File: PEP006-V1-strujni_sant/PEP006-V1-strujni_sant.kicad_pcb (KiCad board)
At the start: 2 copper layers, 45 x 45 mm, 17 parts, among them J1 Screw_Terminal_01x02, J2 Conn_01x02_Pin, J3 Conn_01x02_Pin, J4 Conn_01x02_Pin

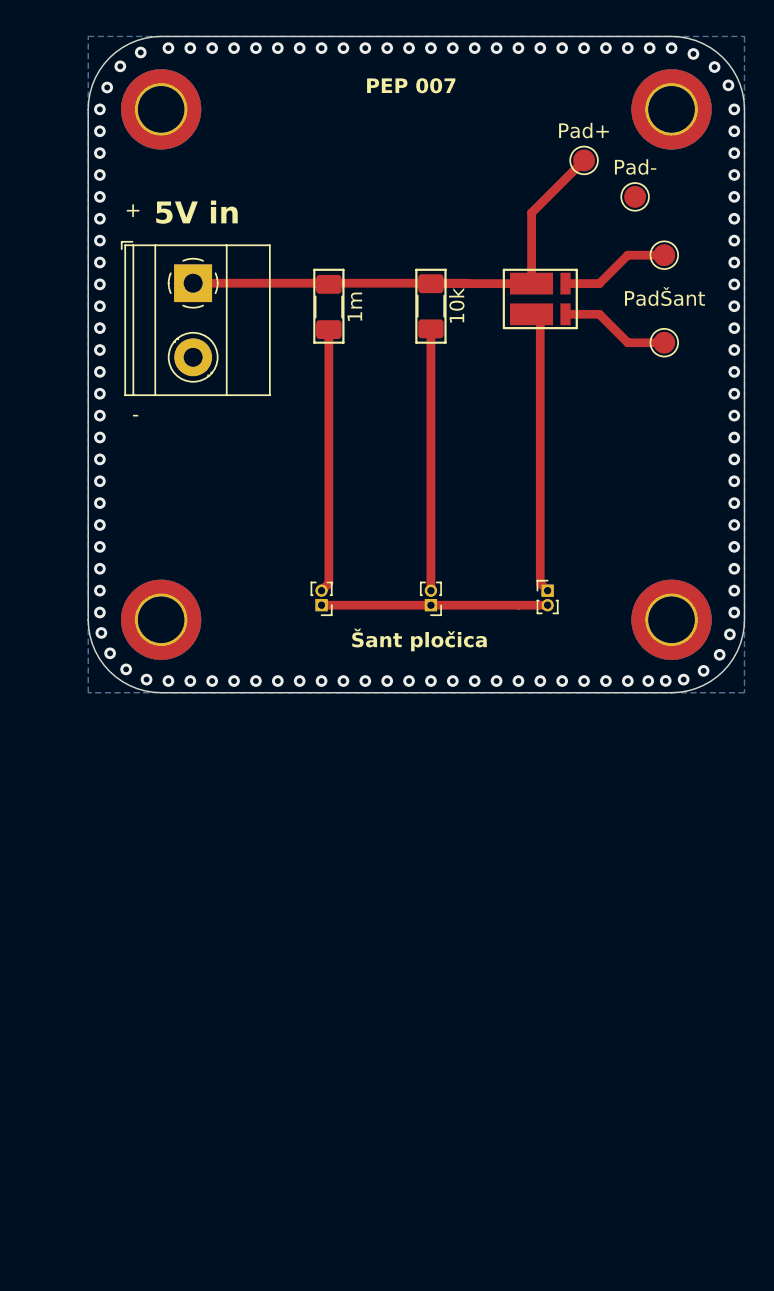
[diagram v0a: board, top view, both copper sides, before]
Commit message: PEP006 and PEP009 update.
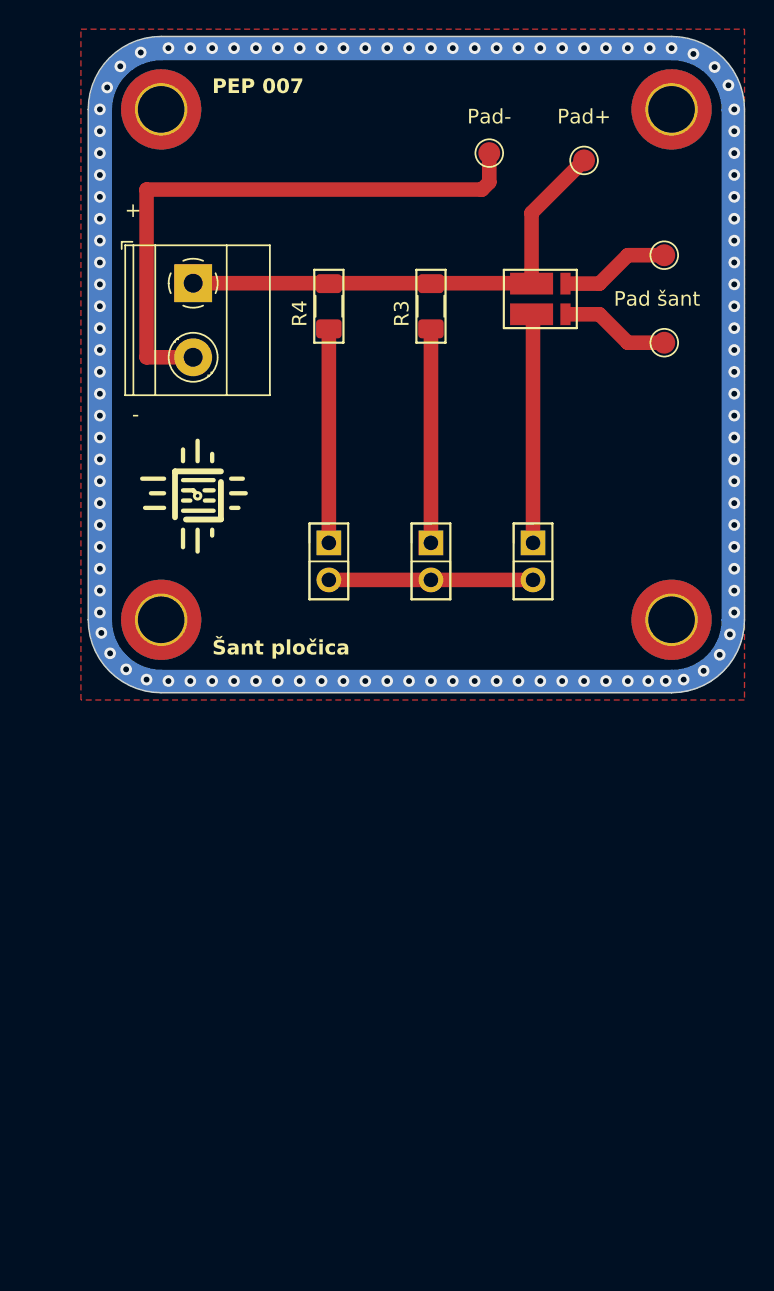
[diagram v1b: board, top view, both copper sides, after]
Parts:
- removed 10k: 10k, Resistor_SMD:R_1206_3216Metric_Pad1.30x1.75mm_HandSolder
- removed 1m: 1m, Resistor_SMD:R_1206_3216Metric_Pad1.30x1.75mm_HandSolder
- removed the G*** at (128.3, 88.6)
- removed J2, J3, J4: Conn_01x02_Pin, Connector_PinHeader_1.00mm:PinHeader_1x02_P1.00mm_Vertical
- removed PadŠant, TP5: TestPointShunt, TestPoint:TestPoint_Pad_D1.5mm
- removed R7: WSK12161, 45x45_template-master:RES_WSK12161L000FEA
- added G***: LOGO, sema:semica, B.Cu at (127.0, 87.0)
- added JP1: Jumper, Connector_PinHeader_2.54mm:PinHeader_1x02_P2.54mm_Vertical, F.Cu at (127.5, 95.7)
- added JP2: Jumper, Connector_PinHeader_2.54mm:PinHeader_1x02_P2.54mm_Vertical, F.Cu at (120.5, 95.7)
- added JP3: Jumper, Connector_PinHeader_2.54mm:PinHeader_1x02_P2.54mm_Vertical, F.Cu at (134.5, 95.7)
- added Pad šant: TestPointShunt, TestPoint:TestPoint_Pad_D1.5mm, F.Cu at (143.5, 82.0)
- added R3: 1m, Resistor_SMD:R_1206_3216Metric_Pad1.30x1.75mm_HandSolder, F.Cu at (127.5, 79.5)
- added R4: 10k, Resistor_SMD:R_1206_3216Metric_Pad1.30x1.75mm_HandSolder, F.Cu at (120.5, 79.5)
- added R5: Shunt, WSK12161L000FEA (1):RES_WSK12161L000FEA, F.Cu at (135.0, 79.0)
- added REF**: ele_petnica_logo, PEP_library:ele_petnica_logo, F.Cu at (111.5, 92.5)
- added TP6: TestPointShunt, TestPoint:TestPoint_Pad_D1.5mm, F.Cu at (143.5, 76.0)
- moved Pad- 10.4 mm to (131.5, 69.0)
- moved G*** 0.50 mm to (112.5, 92.5)
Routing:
- net 0: track 15.5 -> 52.7 mm
- net Net-(JP3-A): track 33.0 -> 54.8 mm
- net Net-(J4-Pin_1): track 19.4 -> 0.00 mm
- net Net-(J2-Pin_2): track 18.2 -> 0.00 mm
- net Net-(J3-Pin_2): track 18.0 -> 0.00 mm
- net Net-(JP2-A): track 0.00 -> 14.7 mm
- net Net-(JP1-A): track 0.00 -> 14.7 mm
- net Net-(R7-Pad4): track 7.58 -> 0.00 mm
- net Net-(R7-Pad1): track 7.58 -> 0.00 mm
- net Input voltage: track 0.00 -> 7.31 mm
- added copper zone on F.Cu, net 0
- removed copper zone on B.Cu, net 0
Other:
- board text removed: "5V in"

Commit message: PEP006 update.
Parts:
- removed Pad šant: TestPointShunt, TestPoint:TestPoint_Pad_D1.5mm
- removed Pad+: TestPoint+, TestPoint:TestPoint_Pad_D1.5mm
- removed Pad-: TestPoint-, TestPoint:TestPoint_Pad_D1.5mm
- removed R5: Shunt, WSK12161L000FEA (1):RES_WSK12161L000FEA
- removed REF**: ele_petnica_logo, PEP_library:ele_petnica_logo
- added R1: Shunt, WSK12161L000FEA (1):RES_WSK12161L000FEA, F.Cu at (135.1, 78.9)
- added TP3: TestPoint+, TestPoint:TestPoint_Pad_D1.5mm, F.Cu at (138.0, 69.5)
- added TP7: TestPointShunt, TestPoint:TestPoint_Pad_D1.5mm, F.Cu at (144.0, 76.0)
- added TP8: TestPoint-, TestPoint:TestPoint_Pad_D1.5mm, F.Cu at (132.0, 69.0)
- R3: value 1m -> 100k
- moved TP6 6.02 mm to (144.0, 82.0)
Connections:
- J1 pad 1: Net-(JP3-A) -> Input voltage
- R3 pad 1: Net-(JP3-A) -> Input voltage
- R4 pad 1: Net-(JP3-A) -> Input voltage
- TP6 pad 1: Input voltage -> Net-(R1-Pad4)
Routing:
- net Net-(JP3-A): track 54.8 -> 15.7 mm
- net Input voltage: track 7.31 -> 31.7 mm
- net 0: track 52.7 -> 70.8 mm
- net Net-(R1-Pad4): track 0.00 -> 7.31 mm
- net Net-(R1-Pad1): track 0.00 -> 7.31 mm
- removed copper zone on F.Cu, net 0

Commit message: PEP006
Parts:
- R1: value Shunt -> 2m
- R3: value 100k -> 100
- R4: value 10k -> 1
- TP3, TP6, TP7, TP8: footprint TestPoint:TestPoint_Pad_D1.5mm -> Connector_PinHeader_2.54mm:PinHeader_1x01_P2.54mm_Vertical
- moved TP8 39.7 mm to (128.0, 108.5)
- moved G*** 39.2 mm to (108.5, 131.5)
- moved G*** 39.2 mm to (123.0, 126.0)
- moved H1 39.2 mm to (105.0, 140.0)
- moved H2 39.2 mm to (105.0, 105.0)
- moved H3 39.2 mm to (140.0, 105.0)
- moved H4 39.2 mm to (140.0, 140.0)
- moved J1 39.2 mm to (107.2, 116.9)
- moved JP1 39.2 mm to (123.5, 134.7)
- moved JP2 39.2 mm to (116.5, 134.7)
- moved JP3 39.2 mm to (130.5, 134.7)
- moved R1 39.2 mm to (131.1, 117.9)
- moved R3 39.2 mm to (123.5, 118.5)
- moved R4 39.2 mm to (116.5, 118.5)
- moved TP3 39.2 mm to (134.0, 108.5)
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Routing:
- net 0: track 70.8 -> 67.4 mm

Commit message: PEP006 final commit, ready for production.
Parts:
- added REF**: ele_petnica_logo, PEP_library:ele_petnica_logo, F.Cu at (111.5, 108.8)

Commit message: PEP006 final.
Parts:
- removed the G*** at (123.0, 126.0)
- added REF**: JP_silk_symbol, PEP_library:JP_silk_symbol, F.Cu at (133.0, 133.5)
- added REF**: JP_silk_symbol, PEP_library:JP_silk_symbol, F.Cu at (126.0, 133.5)
- added REF**: R_silk_symbol, PEP_library:R_silk_symbol, F.Cu at (133.0, 113.5)
- added REF**: R_silk_symbol, PEP_library:R_silk_symbol, F.Cu at (119.0, 113.5)
- added REF**: R_silk_symbol, PEP_library:R_silk_symbol, F.Cu at (126.0, 113.5)
- added REF**: JP_silk_symbol, PEP_library:JP_silk_symbol, F.Cu at (119.0, 133.5)
- moved G*** 1.00 mm to (109.5, 131.5)
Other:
- board text added: "V_{in}"
